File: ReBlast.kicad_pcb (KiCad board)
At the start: 2 copper layers, 52.3 x 51.8 mm, 27 parts, among them J1 MOS_8580_Socket, U1 74HC20, U2 74HC139, U3 ZN428E-8, U4 TLC272, U5 MOS_8580, U6 ADC0804

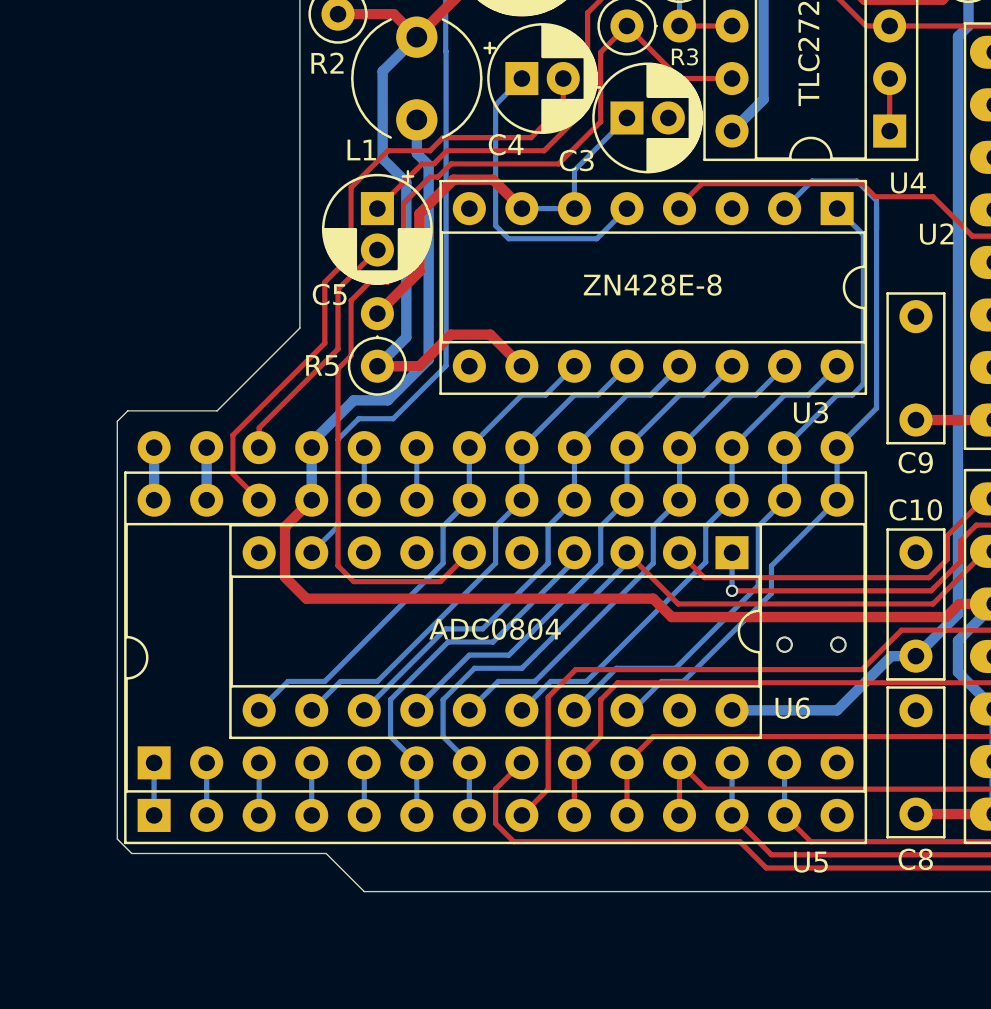
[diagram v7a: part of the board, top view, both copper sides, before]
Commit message: Swap SID socket and connector This is so that the board sits a bit further up the ReBlast card and doesn't hit the computer case
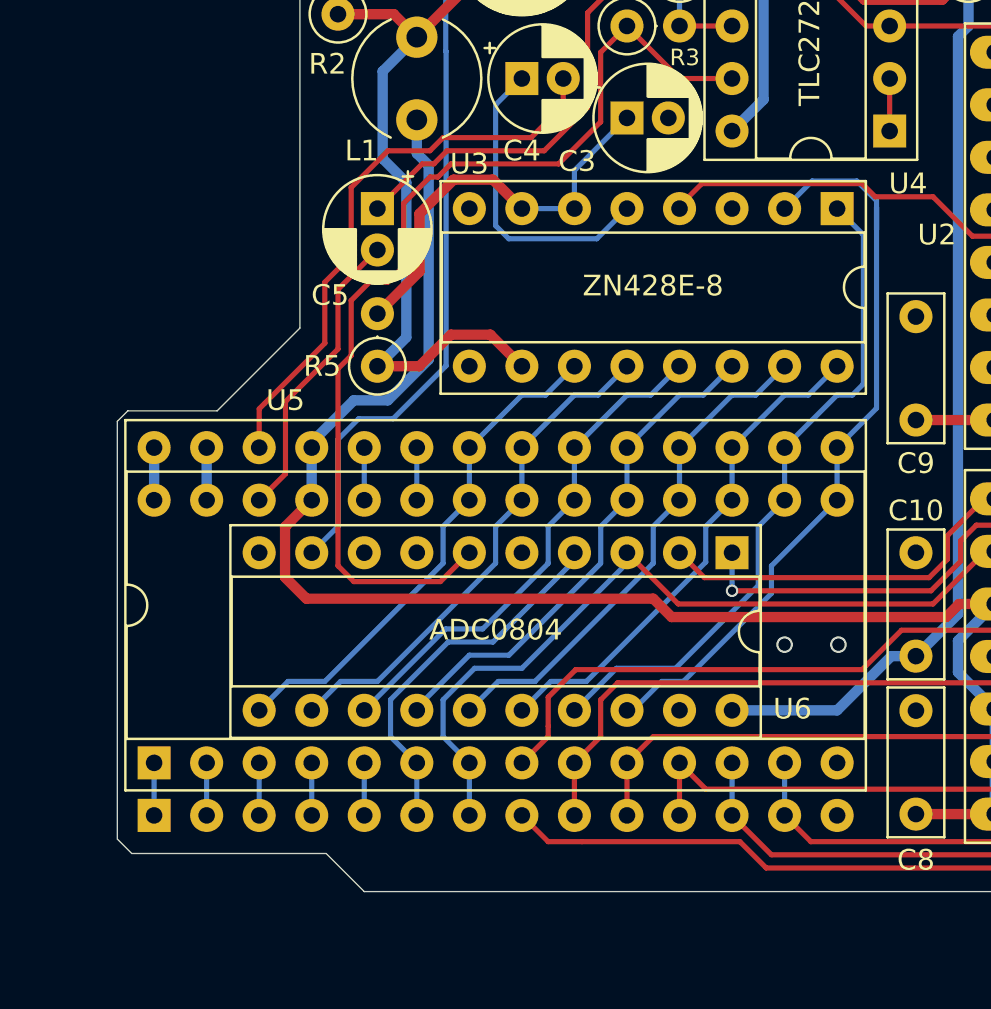
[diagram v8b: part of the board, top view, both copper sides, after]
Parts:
- moved J1 2.54 mm to (128.4, 116.5)
- moved U5 2.54 mm to (128.4, 113.9)
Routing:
- net /~cs_in: track 63.3 -> 58.7 mm
- net /audio_in: track 31.2 -> 27.6 mm
- net /~cs_sid: track 55.3 -> 52.3 mm
- net /audio_jack: track 11.9 -> 14.0 mm
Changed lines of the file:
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@@
     (thickness 1.6)
     (drawings 99)
-    (tracks 349)
+    (tracks 350)
     (zones 0)
     (modules 27)
@@
   (title_block
     (title ReBlast)
-    (date 2024-04-05)
+    (date 2024-08-18)
     (rev 1git)
     (company SukkoPera)
@@
   )
   (module ReBlast:DIP-28_W15.24mm_Socket (layer F.Cu)
-    (at 128.397 113.919 90)
+    (at 128.397 116.459 90)
     (descr "28-lead though-hole mounted DIP package, row spacing 15.24 mm (600 mils)")
     (tags "THT DIP DIL PDIP 2.54mm 15.24mm 600mil")
@@
   )
   (module Package_DIP:DIP-28_W15.24mm_Socket (layer F.Cu)
-    (at 128.397 116.459 90)
+    (at 128.397 113.919 90)
     (descr "28-lead though-hole mounted DIP package, row spacing 15.24 mm (600 mils), Socket")
     (tags "THT DIP DIL PDIP 2.54mm 15.24mm 600mil Socket")
-    (fp_text reference U5 (at -2.286 31.75 180) (layer F.SilkS)
+    (fp_text reference U5 (at 17.526 6.35 180) (layer F.SilkS)
       (effects (font (size 1 1) (thickness 0.15)))
     )
@@
     (descr "16-lead though-hole mounted DIP package, row spacing 7.62 mm (300 mils), Socket")
     (tags "THT DIP DIL PDIP 2.54mm 7.62mm 300mil Socket")
-    (fp_text reference U3 (at 9.904501 1.27 180) (layer F.SilkS)
+    (fp_text reference U3 (at -2.160499 17.78 180) (layer F.SilkS)
       (effects (font (size 1 1) (thickness 0.15)))
     )
@@
     (descr "CP, Radial series, Radial, pin pitch=2.00mm, , diameter=5mm, Electrolytic Capacitor")
     (tags "CP Radial series Radial pin pitch 2.00mm  diameter 5mm Electrolytic Capacitor")
-    (fp_text reference C4 (at -0.762 3.2385) (layer F.SilkS)
+    (fp_text reference C4 (at 0 3.4925) (layer F.SilkS)
       (effects (font (size 1 1) (thickness 0.15)))
     )
@@
   (segment (start 136.652 90.678) (end 137.922 89.408) (width 0.25) (layer F.Cu) (net 18))
   (segment (start 136.652 93.63075) (end 136.652 90.678) (width 0.25) (layer F.Cu) (net 18))
-  (segment (start 132.207 99.949) (end 132.207 98.07575) (width 0.25) (layer F.Cu) (net 18))
-  (segment (start 132.207 98.07575) (end 136.652 93.63075) (width 0.25) (layer F.Cu) (net 18))
-  (segment (start 133.477 101.219) (end 132.207 99.949) (width 0.25) (layer F.Cu) (net 18) (status 10))
+  (segment (start 133.477 96.80575) (end 133.746875 96.535875) (width 0.25) (layer F.Cu) (net 18))
+  (segment (start 133.477 98.679) (end 133.477 96.80575) (width 0.25) (layer F.Cu) (net 18))
+  (segment (start 133.746875 96.535875) (end 136.652 93.63075) (width 0.25) (layer F.Cu) (net 18))
   (via (at 161.4805 108.203) (size 0.8) (drill 0.6) (layers F.Cu B.Cu) (net 19))
   (via (at 158.877 108.203) (size 0.8) (drill 0.6) (layers F.Cu B.Cu) (net 19))
@@
   (segment (start 137.287 91.028499) (end 139.192 89.123499) (width 0.25) (layer F.Cu) (net 23) (status 20))
   (segment (start 137.287 93.9165) (end 137.287 91.028499) (width 0.25) (layer F.Cu) (net 23))
-  (segment (start 133.477 97.7265) (end 137.287 93.9165) (width 0.25) (layer F.Cu) (net 23))
-  (segment (start 133.477 98.679) (end 133.477 97.7265) (width 0.25) (layer F.Cu) (net 23) (status 10))
+  (segment (start 134.747 99.949) (end 133.795205 100.900795) (width 0.25) (layer F.Cu) (net 23))
+  (segment (start 134.747 96.4565) (end 134.747 99.949) (width 0.25) (layer F.Cu) (net 23))
+  (segment (start 134.747 96.4565) (end 137.287 93.9165) (width 0.25) (layer F.Cu) (net 23))
   (segment (start 149.352 77.6605) (end 151.257 75.7555) (width 0.25) (layer F.Cu) (net 24) (status 20))
   (segment (start 149.352 82.2325) (end 149.352 77.6605) (width 0.25) (layer F.Cu) (net 24))
@@
   (segment (start 172.339 97.3455) (end 176.657 97.3455) (width 0.25) (layer F.Cu) (net 31) (status 20))
   (segment (start 157.988 118.999) (end 156.718 117.729) (width 0.25) (layer F.Cu) (net 31))
-  (segment (start 144.907 115.189) (end 146.177 113.919) (width 0.25) (layer F.Cu) (net 31) (status 20))
-  (segment (start 144.907 116.854002) (end 144.907 115.189) (width 0.25) (layer F.Cu) (net 31))
   (segment (start 157.988 118.999) (end 170.815 118.999) (width 0.25) (layer F.Cu) (net 31))
-  (segment (start 145.781998 117.729) (end 144.907 116.854002) (width 0.25) (layer F.Cu) (net 31))
-  (segment (start 156.718 117.729) (end 145.781998 117.729) (width 0.25) (layer F.Cu) (net 31))
   (via (at 171.45 118.364) (size 0.6) (drill 0.4) (layers F.Cu B.Cu) (net 31))
   (segment (start 170.815 118.999) (end 171.45 118.364) (width 0.25) (layer F.Cu) (net 31))
@@
   (segment (start 170.815 117.729) (end 170.815 111.0615) (width 0.25) (layer B.Cu) (net 31))
   (segment (start 171.45 118.364) (end 170.815 117.729) (width 0.25) (layer B.Cu) (net 31))
+  (segment (start 147.447 117.729) (end 146.177 116.459) (width 0.25) (layer F.Cu) (net 31))
+  (segment (start 149.098 117.729) (end 147.447 117.729) (width 0.25) (layer F.Cu) (net 31))
+  (segment (start 156.718 117.729) (end 149.098 117.729) (width 0.25) (layer F.Cu) (net 31))
   (segment (start 141.097 98.6155) (end 141.097 101.1555) (width 0.25) (layer B.Cu) (net 32) (status 30))
   (segment (start 138.557 98.679) (end 138.557 101.219) (width 0.25) (layer B.Cu) (net 33) (status 30))
@@
   (segment (start 171.704 98.806) (end 171.704 106.6165) (width 0.25) (layer B.Cu) (net 42))
   (segment (start 171.704 106.6165) (end 170.815 107.5055) (width 0.25) (layer B.Cu) (net 42))
-  (segment (start 146.177 116.459) (end 147.447 115.189) (width 0.25) (layer F.Cu) (net 42) (status 10))
-  (segment (start 147.447 115.189) (end 147.447 110.744) (width 0.25) (layer F.Cu) (net 42))
   (segment (start 147.447 110.744) (end 148.7805 109.4105) (width 0.25) (layer F.Cu) (net 42))
   (segment (start 148.7805 109.4105) (end 162.6235 109.4105) (width 0.25) (layer F.Cu) (net 42))
   (segment (start 162.6235 109.4105) (end 164.5285 107.5055) (width 0.25) (layer F.Cu) (net 42))
   (segment (start 164.5285 107.5055) (end 170.815 107.5055) (width 0.25) (layer F.Cu) (net 42))
+  (segment (start 147.447 112.649) (end 146.495205 113.600795) (width 0.25) (layer F.Cu) (net 42))
+  (segment (start 147.447 112.141) (end 147.447 112.649) (width 0.25) (layer F.Cu) (net 42))
+  (segment (start 147.447 112.141) (end 147.447 110.744) (width 0.25) (layer F.Cu) (net 42))
   (segment (start 175.387 88.4555) (end 176.657 89.7255) (width 0.25) (layer F.Cu) (net 43) (status 20))
   (segment (start 166.0525 86.5505) (end 167.9575 88.4555) (width 0.25) (layer F.Cu) (net 43))
